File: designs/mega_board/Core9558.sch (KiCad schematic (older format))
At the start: 1 part

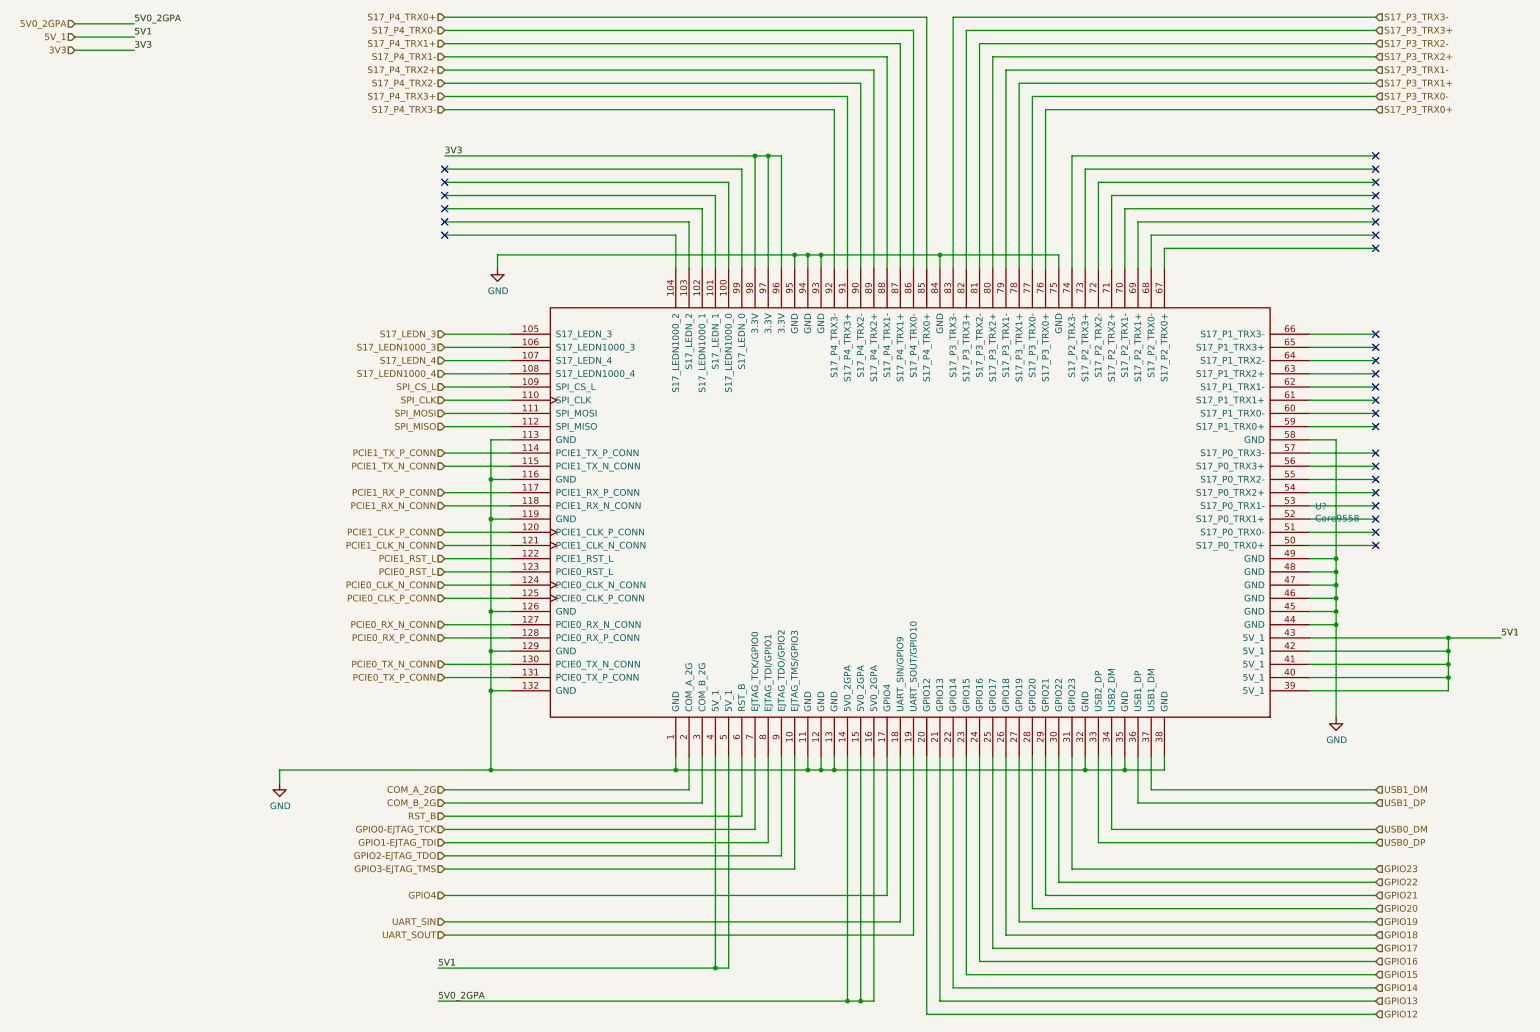
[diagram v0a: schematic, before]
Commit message: Fix 5V1 missleading name
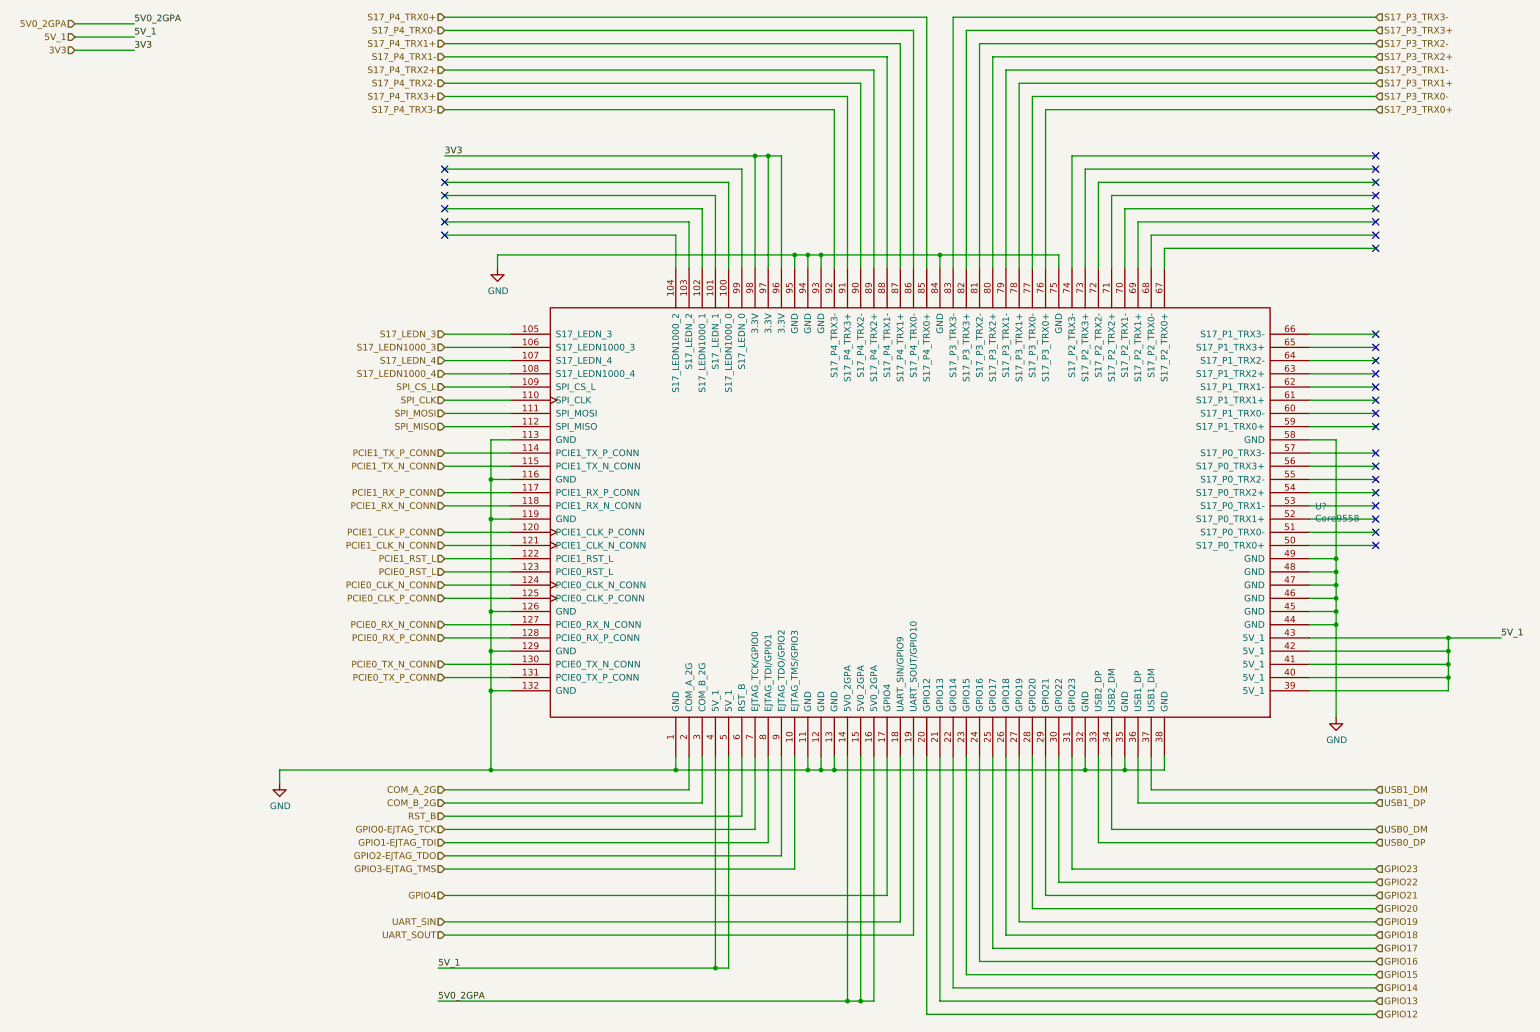
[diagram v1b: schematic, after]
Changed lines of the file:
@@
 5V0_2GPA
 Text Label 13000 5900 0    50   ~ 0
-5V1
+5V_1
 Text Label 2650 1450 0    50   ~ 0
 3V3
@@
 5V0_2GPA
 Text Label 4950 8400 0    50   ~ 0
-5V1
+5V_1
 Wire Wire Line
 	11750 5300 11750 4400
@@
 3V3
 Text Label 2650 1350 0    50   ~ 0
-5V1
+5V_1
 Wire Wire Line
 	5500 4400 5350 4400

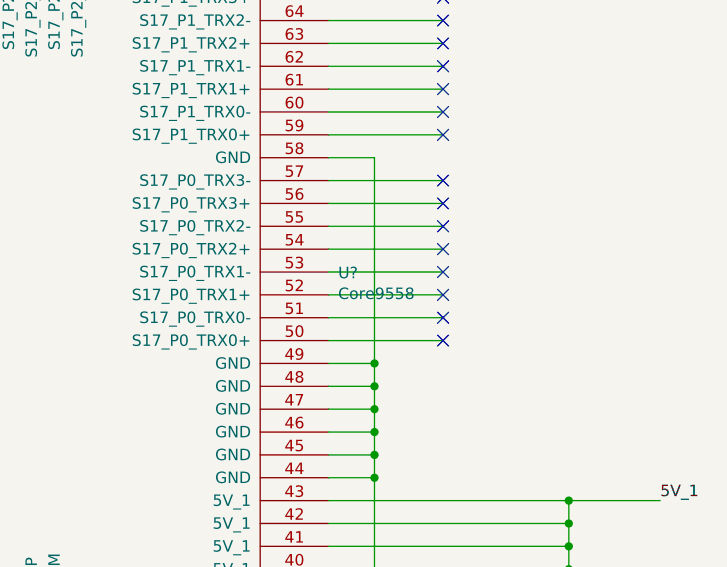
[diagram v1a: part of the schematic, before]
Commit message: Enumerate components as is in eagle design.
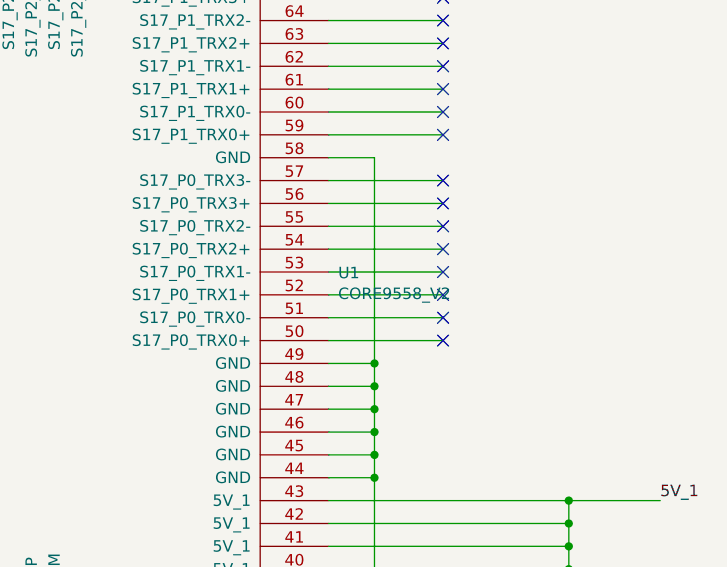
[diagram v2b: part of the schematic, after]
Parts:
- U1: renamed from U?; value Core9558 -> CORE9558_V2; footprint MODULE -> LibreRouter_MegaBoard:DRAGINO_CORE9558
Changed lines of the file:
@@
 Connection ~ 8750 3000
 $Comp
-L power:GND #PWR?
+L power:GND #PWR0121
 U 1 1 5D233379
 P 5400 3100
-F 0 "#PWR?" H 5400 2850 50  0001 C CNN
+F 0 "#PWR0121" H 5400 2850 50  0001 C CNN
 F 1 "GND" H 5405 2927 50  0000 C CNN
 F 2 "" H 5400 3100 50  0001 C CNN
@@
 	11750 5800 11750 6500
 $Comp
-L power:GND #PWR?
+L power:GND #PWR0122
 U 1 1 5D27B8DD
 P 11750 6500
-F 0 "#PWR?" H 11750 6250 50  0001 C CNN
+F 0 "#PWR0122" H 11750 6250 50  0001 C CNN
 F 1 "GND" H 11755 6327 50  0000 C CNN
 F 2 "" H 11750 6500 50  0001 C CNN
@@
 	9850 6900 7950 6900
 $Comp
-L power:GND #PWR?
+L power:GND #PWR0123
 U 1 1 5D310B9F
 P 3750 7000
-F 0 "#PWR?" H 3750 6750 50  0001 C CNN
+F 0 "#PWR0123" H 3750 6750 50  0001 C CNN
 F 1 "GND" H 3755 6827 50  0000 C CNN
 F 2 "" H 3750 7000 50  0001 C CNN
@@
 	7750 3000 7850 3000
 $Comp
-L Core9558:Core9558 U?
+L Core9558:Core9558 U1
 U 1 1 5D47B6E1
 P 8600 4950
-F 0 "U?" H 11591 4996 50  0000 L CNN
-F 1 "Core9558" H 11591 4905 50  0000 L CNN
-F 2 "MODULE" H 8600 4600 50  0001 C CNN
+F 0 "U1" H 11591 4996 50  0000 L CNN
+F 1 "CORE9558_V2" H 11591 4905 50  0000 L CNN
+F 2 "LibreRouter_MegaBoard:DRAGINO_CORE9558" H 8600 4600 50  0001 C CNN
 F 3 "DOCUMENTATION" H 8600 4700 50  0001 C CNN
 	1    8600 4950

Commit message: Add BOM definition for components. We need more iformation for all the components that are not defined.
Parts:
- U1: DNP (none) -> DNP
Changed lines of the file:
@@
 F 2 "LibreRouter_MegaBoard:DRAGINO_CORE9558" H 8600 4600 50  0001 C CNN
 F 3 "DOCUMENTATION" H 8600 4700 50  0001 C CNN
+F 4 "DNP" H 8600 4950 50  0001 C CNN "DNP"
 	1    8600 4950
 	1    0    0    -1

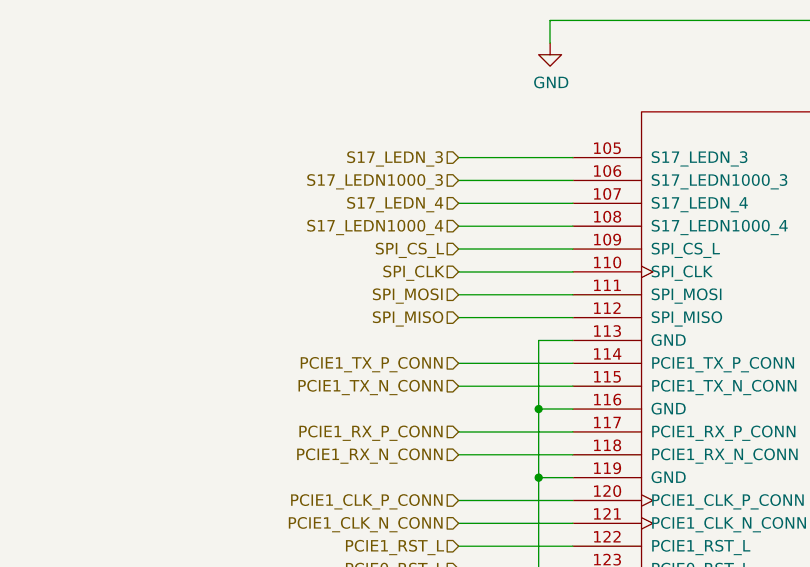
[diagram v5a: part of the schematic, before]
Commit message: Remove spi watchdog erroneous connection
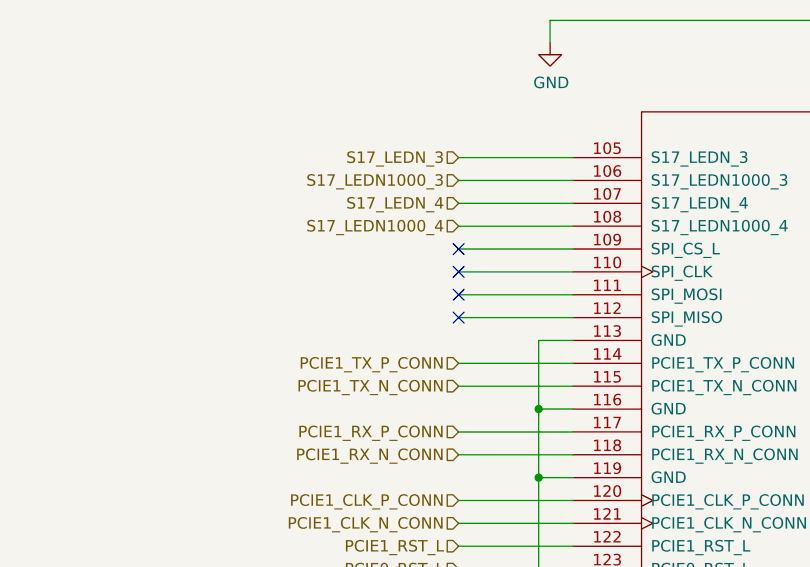
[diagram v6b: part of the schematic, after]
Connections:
- net SPI_CLK: no longer names the net of U1.110 (SPI_CLK)
- net SPI_CS_L: no longer names the net of U1.109 (SPI_CS_L)
- net SPI_MISO: no longer names the net of U1.112 (SPI_MISO)
- net SPI_MOSI: no longer names the net of U1.111 (SPI_MOSI)
- no-connect marks 30 -> 34
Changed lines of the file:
@@
 Wire Wire Line
 	7250 2350 7250 3100
-Text HLabel 5000 4000 0    50   Input ~ 0
-SPI_CS_L
-Text HLabel 5000 4100 0    50   Input ~ 0
-SPI_CLK
-Text HLabel 5000 4200 0    50   Input ~ 0
-SPI_MOSI
-Text HLabel 5000 4300 0    50   Input ~ 0
-SPI_MISO
 Wire Wire Line
 	5000 4500 5500 4500
@@
 Wire Wire Line
 	7650 3000 7750 3000
+NoConn ~ 5000 4000
+NoConn ~ 5000 4100
+NoConn ~ 5000 4200
+NoConn ~ 5000 4300
 $EndSCHEMATC

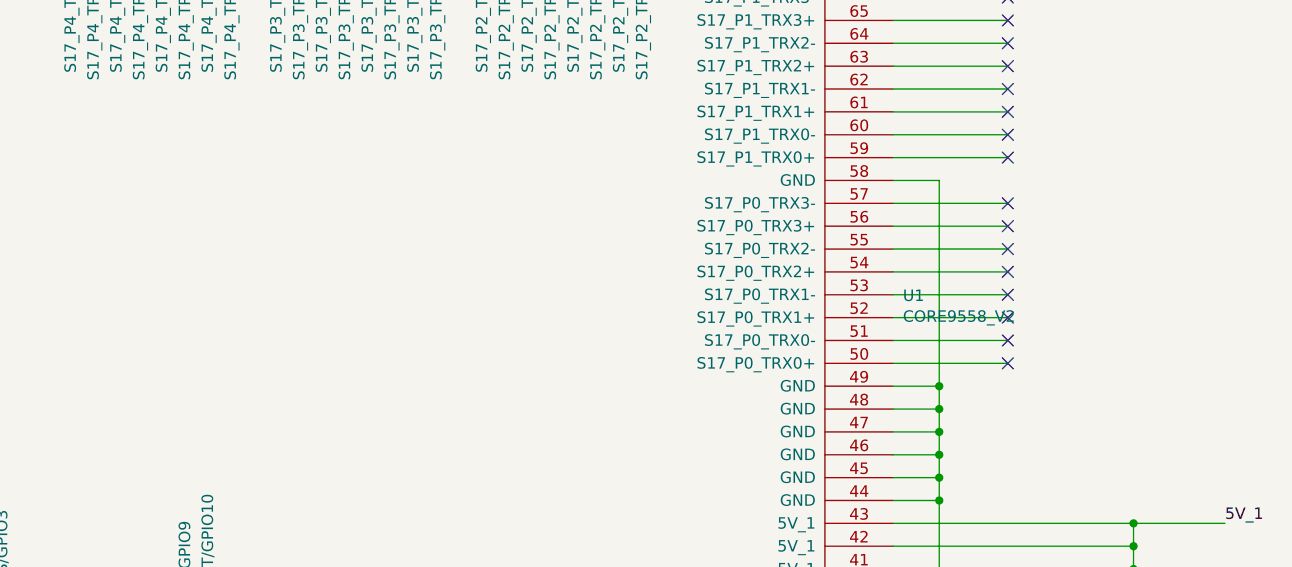
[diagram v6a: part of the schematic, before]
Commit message: Add hack ethernet connector
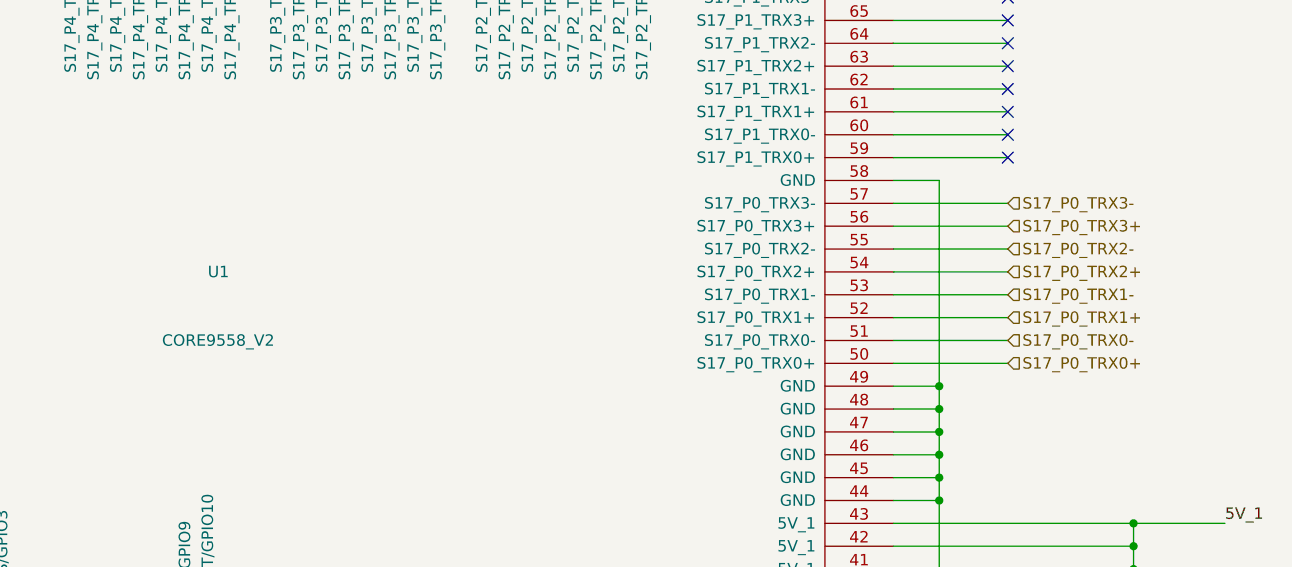
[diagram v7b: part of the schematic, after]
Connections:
- net S17_P0_TRX0+: now reaches U1.50 (S17_P0_TRX0+)
- net S17_P0_TRX0-: now reaches U1.51 (S17_P0_TRX0-)
- net S17_P0_TRX1+: now reaches U1.52 (S17_P0_TRX1+)
- net S17_P0_TRX1-: now reaches U1.53 (S17_P0_TRX1-)
- net S17_P0_TRX2+: now reaches U1.54 (S17_P0_TRX2+)
- net S17_P0_TRX2-: now reaches U1.55 (S17_P0_TRX2-)
- net S17_P0_TRX3+: now reaches U1.56 (S17_P0_TRX3+)
- net S17_P0_TRX3-: now reaches U1.57 (S17_P0_TRX3-)
- no-connect marks 34 -> 26
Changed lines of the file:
@@
 NoConn ~ 12050 4200
 NoConn ~ 12050 4300
-NoConn ~ 12050 5200
-NoConn ~ 12050 5100
-NoConn ~ 12050 5000
-NoConn ~ 12050 4900
-NoConn ~ 12050 4800
-NoConn ~ 12050 4700
-NoConn ~ 12050 4600
-NoConn ~ 12050 4500
 Text HLabel 2200 1250 0    50   Input ~ 0
 5V0_2GPA
@@
 U 1 1 5D47B6E1
 P 8600 4950
-F 0 "U1" H 11591 4996 50  0000 L CNN
-F 1 "CORE9558_V2" H 11591 4905 50  0000 L CNN
+F 0 "U1" H 8550 5100 50  0000 L CNN
+F 1 "CORE9558_V2" H 8350 4800 50  0000 L CNN
 F 2 "LibreRouter_MegaBoard:DRAGINO_CORE9558" H 8600 4600 50  0001 C CNN
 F 3 "DOCUMENTATION" H 8600 4700 50  0001 C CNN
@@
 NoConn ~ 5000 4200
 NoConn ~ 5000 4300
+Text HLabel 12050 5200 2    50   Input ~ 0
+S17_P0_TRX0+
+Text HLabel 12050 5100 2    50   Input ~ 0
+S17_P0_TRX0-
+Text HLabel 12050 5000 2    50   Input ~ 0
+S17_P0_TRX1+
+Text HLabel 12050 4900 2    50   Input ~ 0
+S17_P0_TRX1-
+Text HLabel 12050 4800 2    50   Input ~ 0
+S17_P0_TRX2+
+Text HLabel 12050 4700 2    50   Input ~ 0
+S17_P0_TRX2-
+Text HLabel 12050 4600 2    50   Input ~ 0
+S17_P0_TRX3+
+Text HLabel 12050 4500 2    50   Input ~ 0
+S17_P0_TRX3-
 $EndSCHEMATC
